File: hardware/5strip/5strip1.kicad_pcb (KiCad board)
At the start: 2 copper layers, 76 parts, among them P1 CONN_4, P2 USB_MICRO-B, P3 CONN_4, P4 CONN_2, P5 CONN_4, P6 CONN_4, P7 CONN_4, P8 CONN_6, Q1 NPN, Q10 MOS_N_GDS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

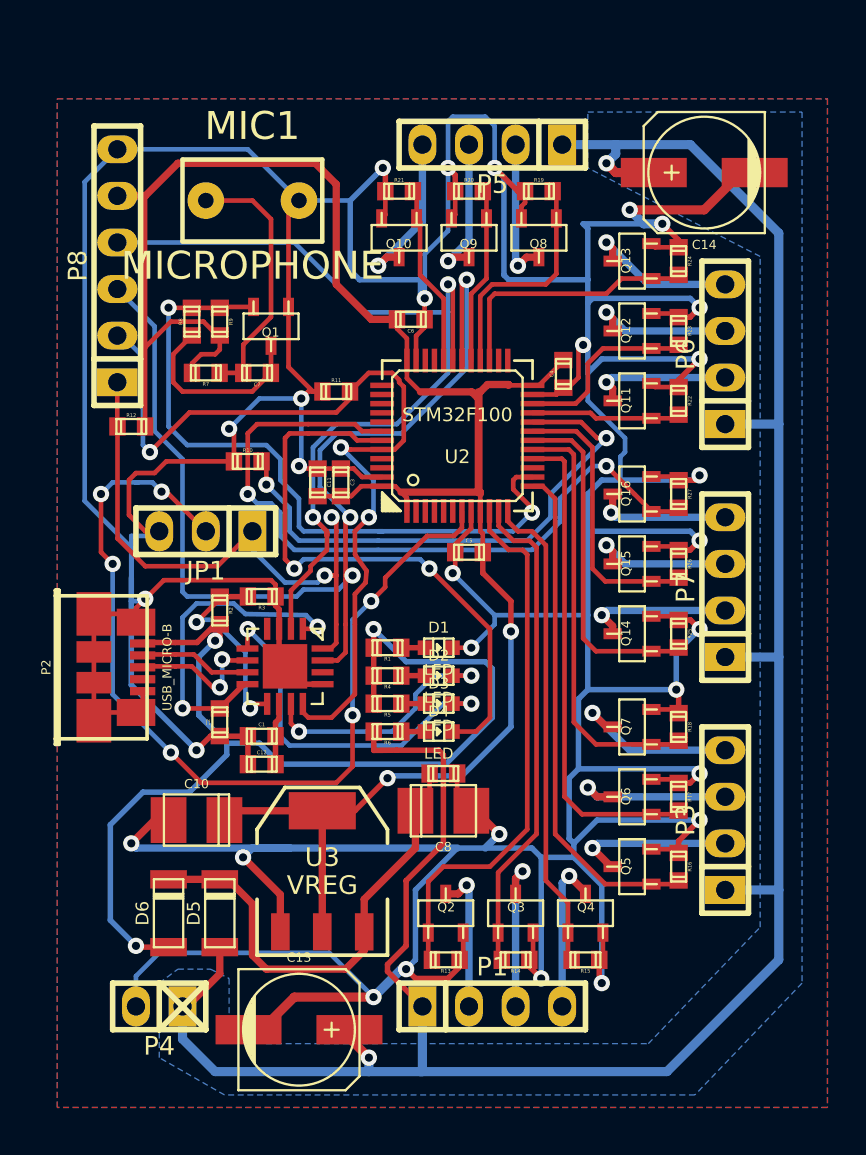
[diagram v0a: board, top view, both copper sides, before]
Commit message: Updated timer registers in rxlamp code
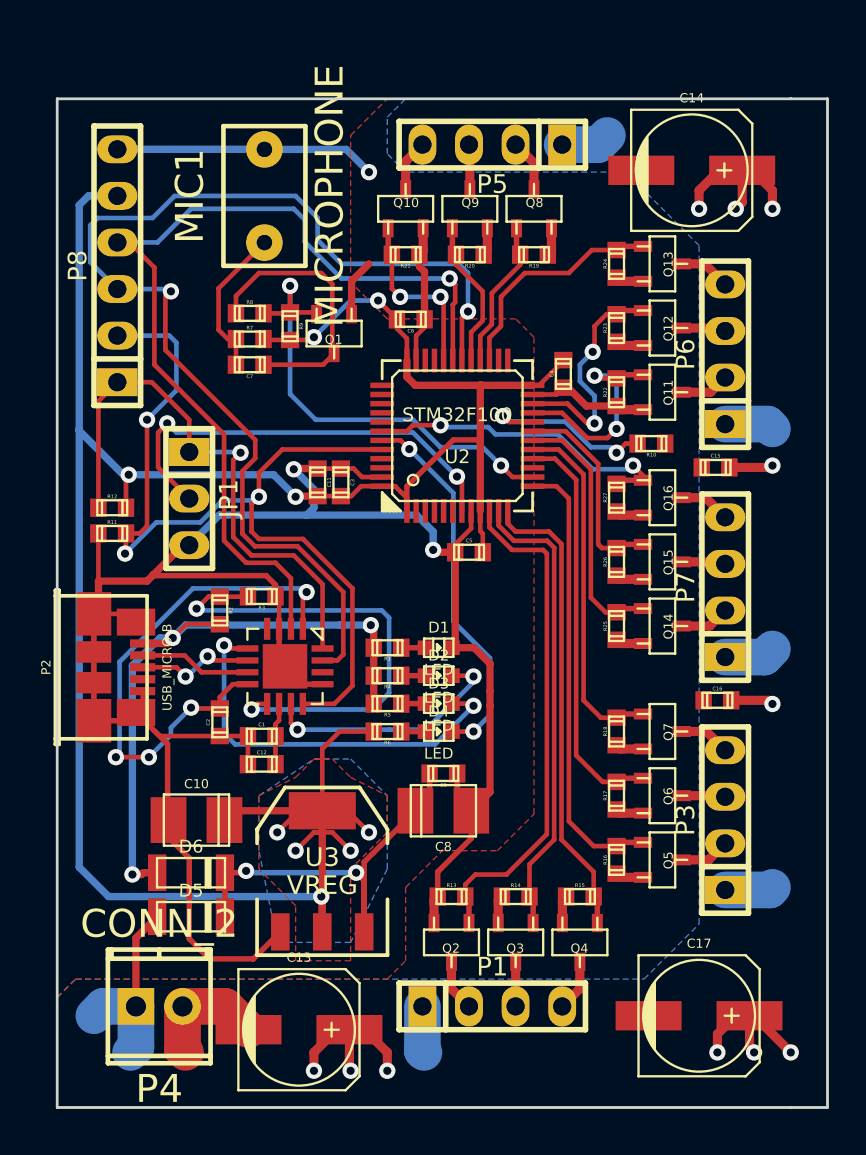
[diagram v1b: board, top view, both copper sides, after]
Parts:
- added C15: C, c_0603, F.Cu at (97.9, 81.1)
- added C16: C, c_0603, F.Cu at (98.0, 93.8)
- added C17: CP, c_elec_6.3x7.7, F.Cu at (97.0, 111.0)
- P4: footprint pin_strip_2 -> mpt_0,5/2-2,54
- moved R10 22.0 mm to (94.4, 79.8), turned to 180 degrees
- moved R11 14.5 mm to (65.0, 84.7)
- moved R12 4.55 mm to (65.0, 83.3)
- moved R9 3.84 mm to (74.7, 73.4)
- moved R21 3.48 mm to (81.0, 69.5), turned to 180 degrees
- moved R19 3.47 mm to (88.0, 69.5), turned to 180 degrees
- moved R13 3.46 mm to (83.5, 104.5), turned to 0 degrees
- moved R15 3.46 mm to (90.5, 104.5), turned to 0 degrees
- moved Q1 3.46 mm to (77.1, 73.8)
- moved R20 3.46 mm to (84.5, 69.5), turned to 180 degrees
- moved R14 3.45 mm to (87.0, 104.5), turned to 0 degrees
- moved R22 3.42 mm to (92.5, 77.0), turned to 90 degrees
- moved R25 3.41 mm to (92.5, 89.8), turned to 90 degrees
- moved R16 3.41 mm to (92.5, 102.5), turned to 90 degrees
- moved R18 3.39 mm to (92.5, 95.5), turned to 90 degrees
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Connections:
- R6 pad 1: /V_EXT -> /VCC_3V3
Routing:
- net GND: track 426.0 -> 183.4 mm, vias 29 -> 3
- net /V_EXT: track 135.1 -> 55.3 mm, vias 2 -> 11
- net N-0000042: track 51.1 -> 24.0 mm, vias 6 -> 2
- net /VCC_3V3: track 117.6 -> 142.8 mm, vias 2 -> 9
- net /V_USB: track 59.9 -> 35.7 mm
- net /3ch_fetdriver_5/D2: track 40.3 -> 17.4 mm
- net /BOOT1: track 29.7 -> 10.1 mm
- net N-0000048: track 11.1 -> 26.7 mm
- net /MIC: track 38.9 -> 25.4 mm
- net /DEBUG_LED: track 32.5 -> 20.4 mm
- net N-0000027: track 18.1 -> 28.8 mm, vias 2 -> 4
- net /3ch_fetdriver_2/Q1: track 9.27 -> 2.39 mm, vias 1 -> 0
- net /3ch_fetdriver_2/Q2: track 9.50 -> 2.79 mm, vias 1 -> 0
- net /3ch_fetdriver_1/Q1: track 8.91 -> 2.44 mm, vias 1 -> 0
- net /3ch_fetdriver_2/Q0: track 8.87 -> 2.74 mm, vias 1 -> 0
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- added copper zone on B.Cu, net /VCC_3V3
- added copper zone on F.Cu, net GND
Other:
- board outline added: 42 x 55 mm
